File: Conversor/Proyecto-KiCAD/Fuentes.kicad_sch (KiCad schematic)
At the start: 17 parts, among them U11 LM7805_TO252, U13 THB3-1211

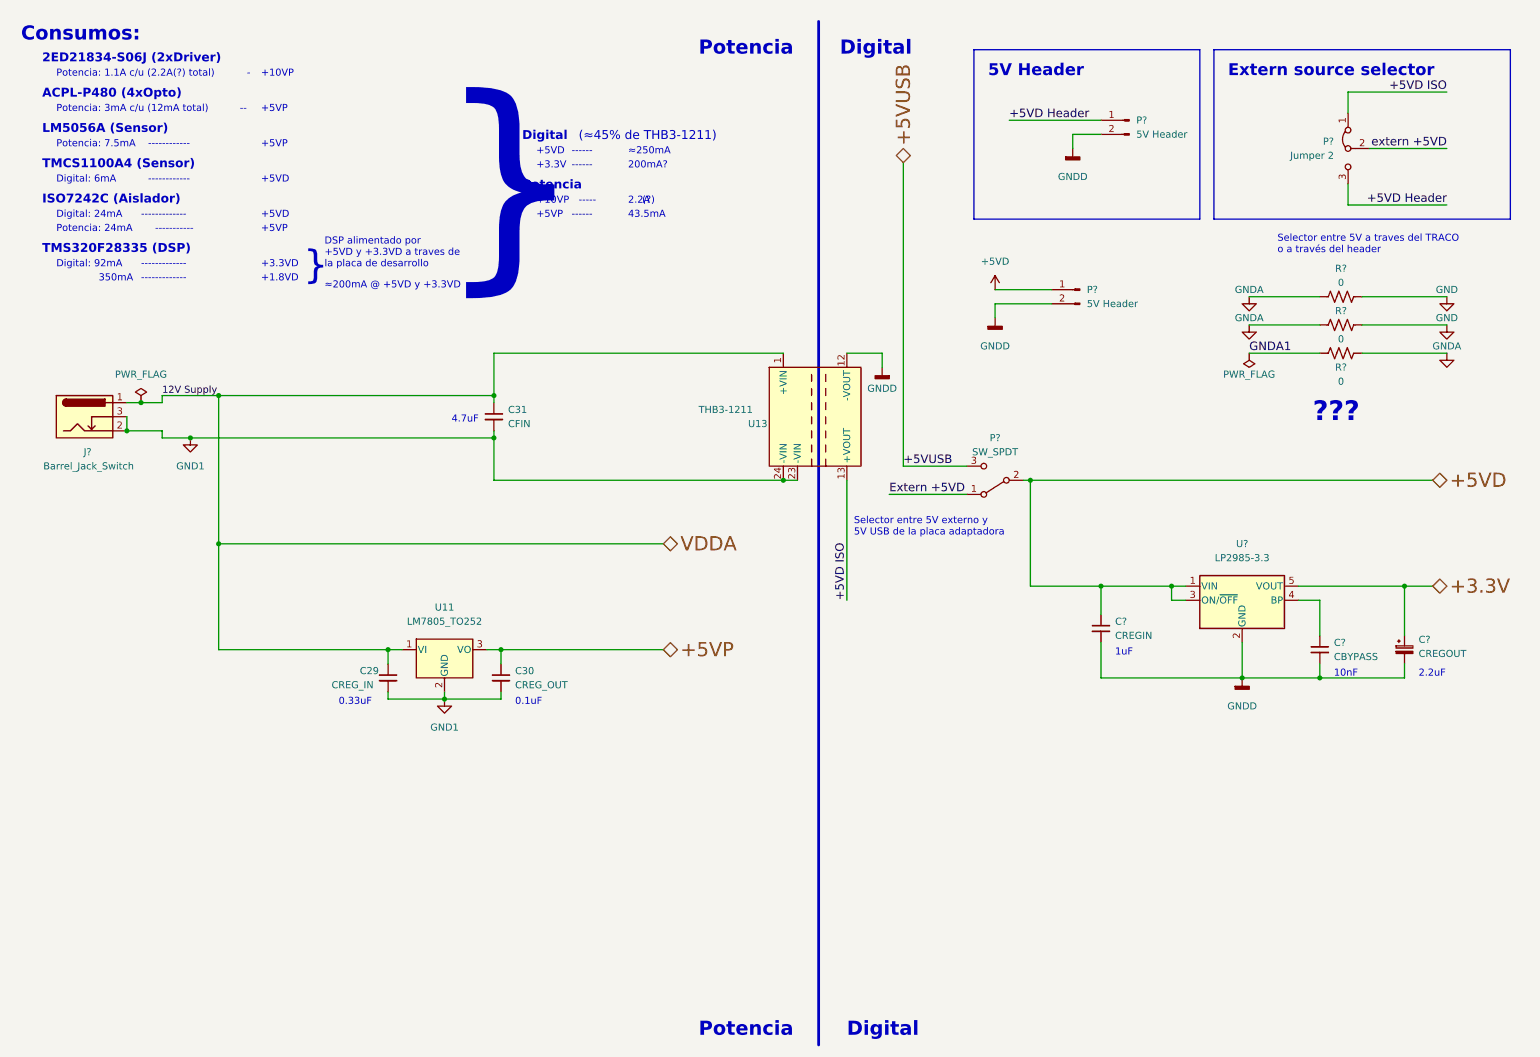
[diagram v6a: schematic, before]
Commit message: Arreglar todos los errores del ERC
- Agregar flags de 'Not Connected' a pines flotantes
- Agregar resistencias 'falsas' para eliminar los errores de 'Power
input pin not connected to Power output pin'
- Agregar un GND1 conectado a PWR_FLAG para arreglar errores
- Además, agregar bien al proyecto la placa adaptadora importada a KiCad
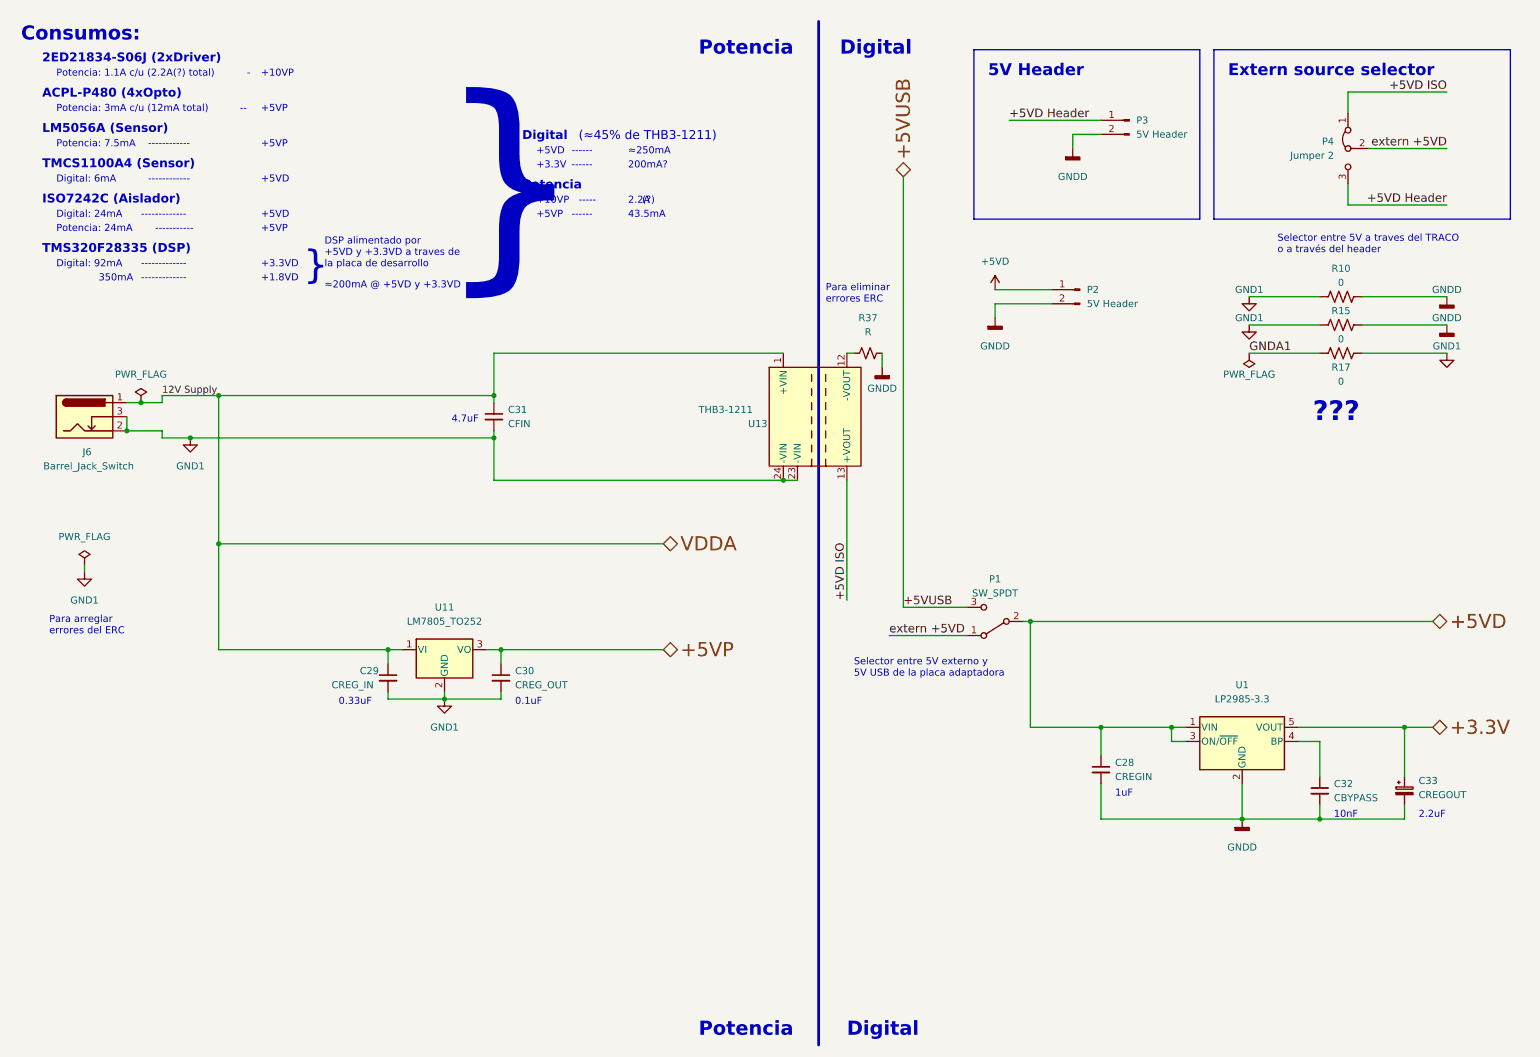
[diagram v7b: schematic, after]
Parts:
- added R37: R, symbol Device:R_Small_US
- gave numbers to parts that had none: 12
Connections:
- net Extern +5VD is gone; now on net extern +5VD: P1.1 (A)
- net GND1: now also R10.1, R15.1, R17.2
- net GNDD: now also R10.2, R15.2, R37.2; no longer U13.12 (-VOUT)
- removed net GND: R10.1, R10.2, R15.1, R15.2, R17.2
- new net: R37.1, U13.12 (-VOUT)
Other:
- note added: "Para arreglar errores del ERC"
- note added: "Para eliminar errores ERC"
- moved on the sheet: C28, C32, C33, P1, U1

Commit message: Comenzar a asignar footprints a todos los componentes
- Agregado un header para conectar el módulo de tarjeta SD de Arduino
por SPI
- Los GNDs conectados por resistencias nulas son para conectar los GNDs
en caso de que fuera necesario
- Agregar una nota de aplicaión de aislación para I2C (creo que como
estan conectados SDAO y SDAI está bien)
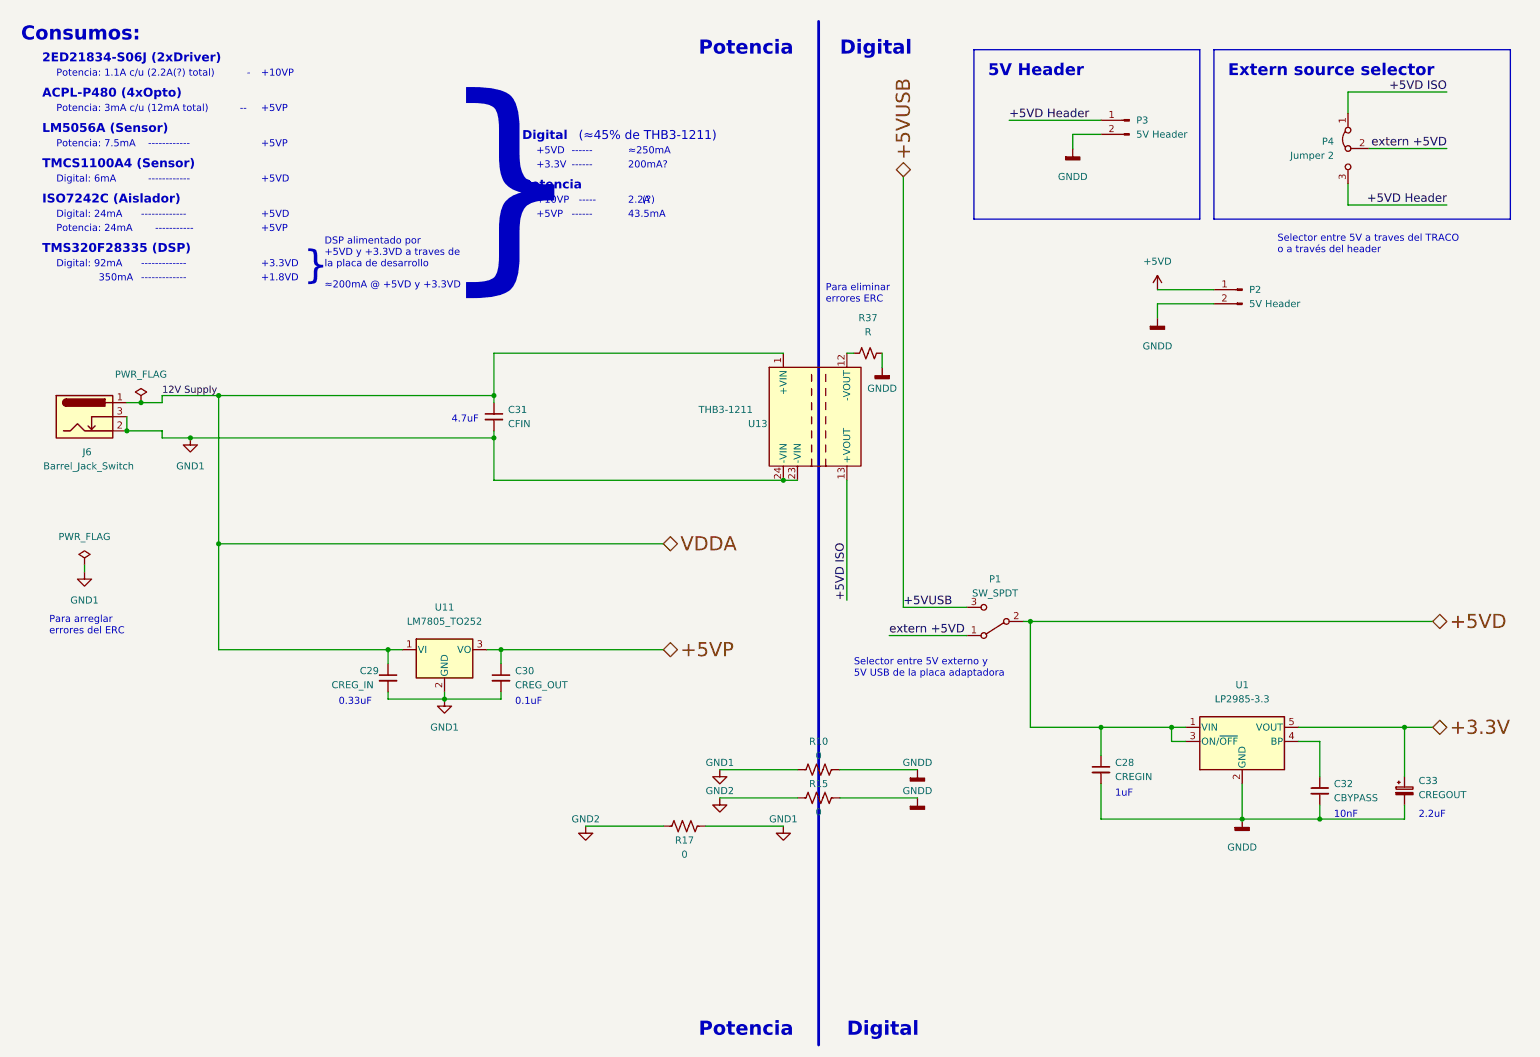
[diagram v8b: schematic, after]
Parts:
- C32: footprint (none) -> Capacitor_SMD:C_1206_3216Metric_Pad1.33x1.80mm_HandSolder
- P2, P3: footprint (none) -> Connector_PinHeader_2.54mm:PinHeader_1x02_P2.54mm_Vertical
- P4: footprint (none) -> Connector_PinHeader_2.54mm:PinHeader_1x03_P2.54mm_Vertical
- U13: footprint (none) -> Package_DIP:DIP-24_W15.24mm
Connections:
- net GND1: no longer R15.1
- net GNDA1 renamed GND2
- net GND2: now also R15.1
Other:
- note removed: "???"
- moved on the sheet: P2, R10, R15, R17
